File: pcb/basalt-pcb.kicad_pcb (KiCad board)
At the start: 2 copper layers, 29 x 42 mm, 12 parts, among them J1 Conn_01x07_Pin, J2 Conn_01x07_Pin, J3 USB4215-03-A, J4 Conn_01x04_Pin, U1 DI78L3.3ZAB, U2 STM32C071F8Px

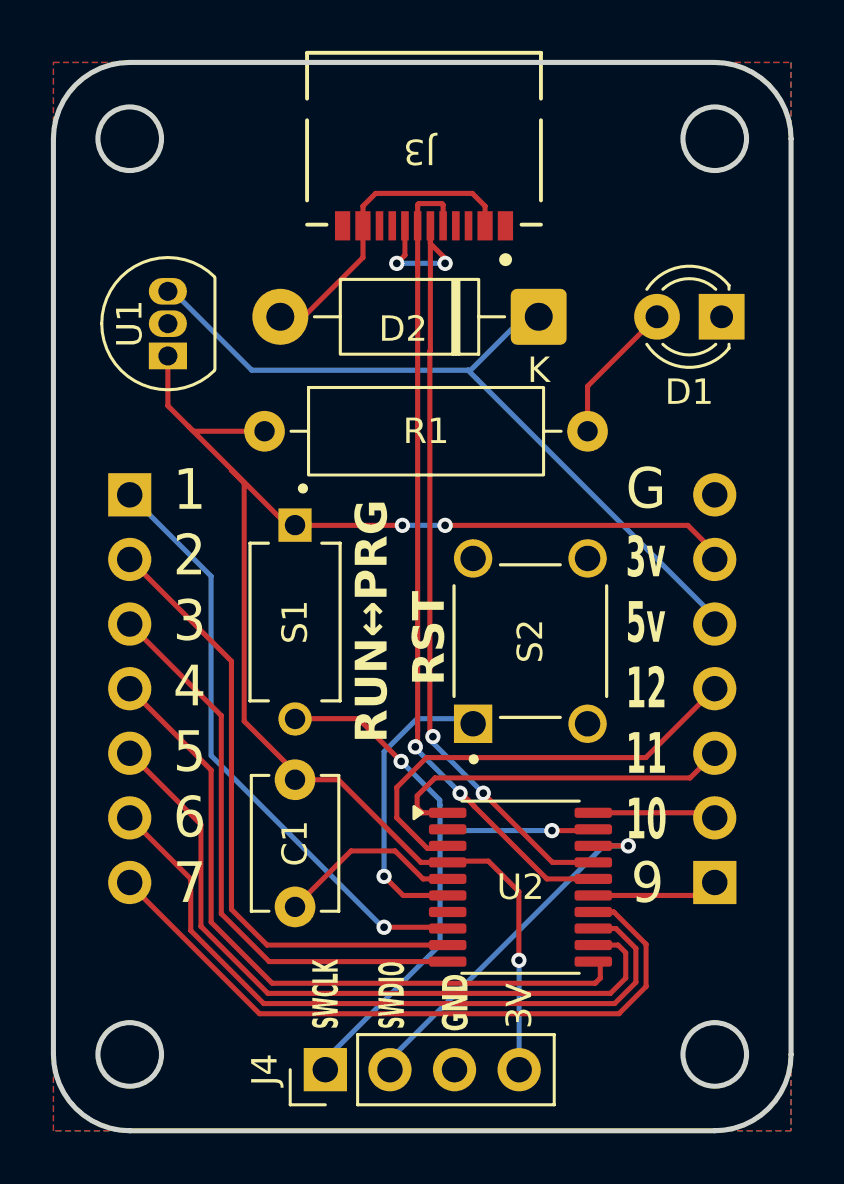
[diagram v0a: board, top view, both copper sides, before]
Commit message: Switch to using STM32C071G8U6 that is supported by STM32duino currently
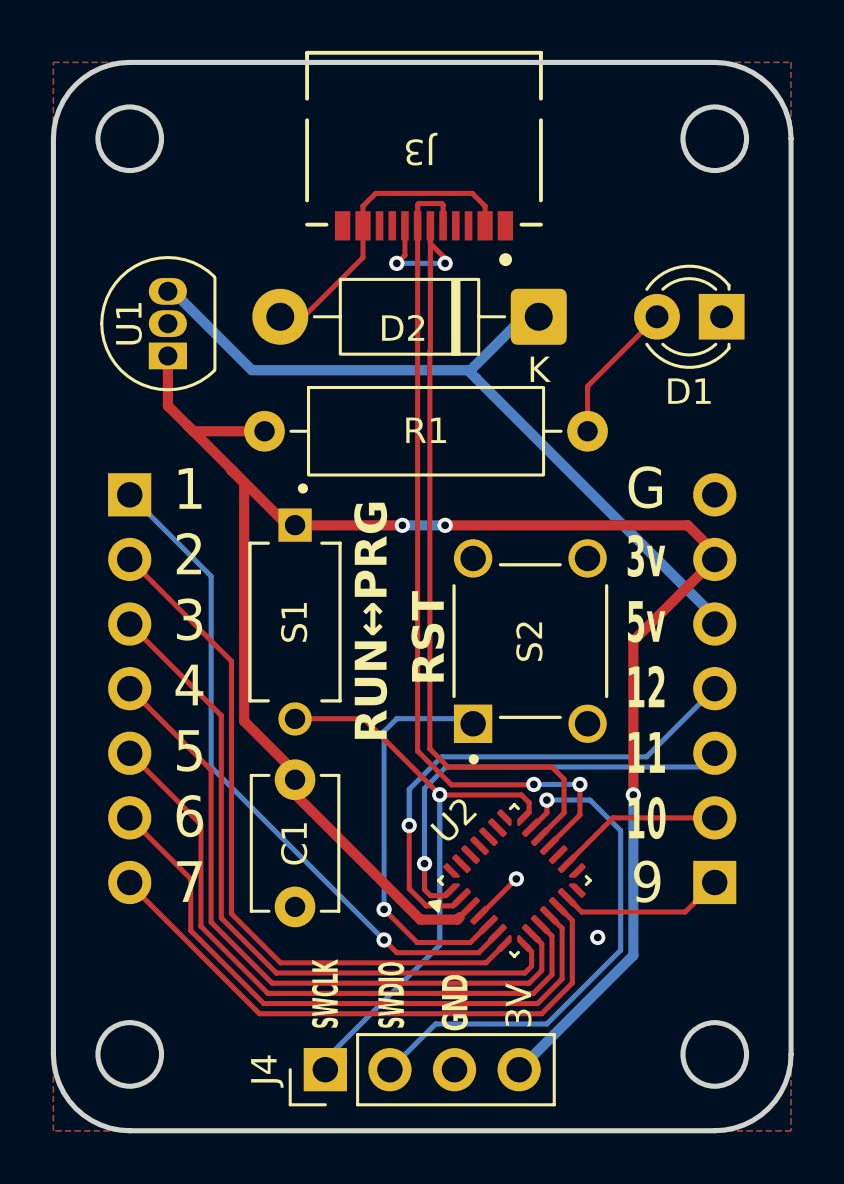
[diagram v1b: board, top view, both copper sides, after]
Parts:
- U2: footprint Package_SO:TSSOP-20_4.4x6.5mm_P0.65mm -> Package_DFN_QFN:QFN-28_4x4mm_P0.5mm
- moved U2 0.36 mm to (153.1, 109.2), turned to 45 degrees
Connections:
- U2 pad 10: Net-(J1-Pin_3) -> Net-(J1-Pin_5)
- U2 pad 11: Net-(J1-Pin_4) -> Net-(J1-Pin_6)
- U2 pad 12: Net-(J1-Pin_5) -> Net-(J1-Pin_7)
- U2 pad 13: Net-(J1-Pin_6) -> Net-(J2-Pin_1)
- U2 pad 14: Net-(J1-Pin_7) -> unconnected-(U2-PB0-Pad14)
- U2 pad 15: Net-(J2-Pin_1) -> unconnected-(U2-PB1-Pad15)
- U2 pad 16: Net-(J3-DN1) -> Net-(J2-Pin_2)
- U2 pad 17: Net-(J3-DP1) -> unconnected-(U2-PC6-Pad17)
- U2 pad 18: Net-(J4-Pin_2) -> Net-(J3-DN1)
- U2 pad 19: Net-(J4-Pin_1) -> Net-(J3-DP1)
- U2 pad 2: unconnected-(U2-PC14-Pad2) -> Net-(J2-Pin_4)
- U2 pad 20: Net-(J2-Pin_2) -> Net-(J4-Pin_2)
- U2 pad 3: Net-(J2-Pin_4) -> +3.3V
- U2 pad 4: +3.3V -> GND
- U2 pad 5: GND -> Net-(U2-PF2)
- U2 pad 6: Net-(U2-PF2) -> Net-(J1-Pin_1)
- U2 pad 7: unconnected-(U2-PA0-Pad7) -> Net-(J1-Pin_2)
- U2 pad 8: Net-(J1-Pin_1) -> Net-(J1-Pin_3)
- U2 pad 9: Net-(J1-Pin_2) -> Net-(J1-Pin_4)
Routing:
- net +3.3V: track 60.5 -> 75.2 mm
- net Net-(J4-Pin_2): track 14.8 -> 20.5 mm
- net GND: track 7.37 -> 2.04 mm, vias 0 -> 2
- net Net-(J1-Pin_3): track 22.9 -> 27.6 mm
- net Net-(U2-PF2): track 11.8 -> 15.7 mm
- net Net-(J1-Pin_7): track 27.7 -> 23.9 mm
- net Net-(J1-Pin_5): track 28.9 -> 25.3 mm
- net Net-(J1-Pin_6): track 27.9 -> 24.4 mm
- net Net-(J2-Pin_3): track 14.3 -> 17.3 mm, vias 0 -> 1
- net Net-(J1-Pin_2): track 24.5 -> 27.5 mm
- net Net-(J1-Pin_1): track 23.7 -> 26.6 mm
- net Net-(J2-Pin_4): track 17.8 -> 20.0 mm, vias 0 -> 1
- net Net-(J2-Pin_2): track 5.05 -> 7.02 mm
- net Net-(J4-Pin_1): track 25.8 -> 24.1 mm, vias 2 -> 1
- net Net-(J1-Pin_4): track 28.2 -> 26.5 mm
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
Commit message: Small pcb tweaks
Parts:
- J3: footprint footprints2:CONN_8p94X6p5X3p16_12L_GCC -> my-kicad-parts:USB4215-03-A
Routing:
- net +5V: track 30.5 -> 31.4 mm
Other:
- board text added: "Basalt Rev2"
- board text added: "github.com/oc-ece-mesa"
